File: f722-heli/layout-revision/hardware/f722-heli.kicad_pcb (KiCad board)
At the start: 6 copper layers, 41.7 x 25.4 mm, 156 parts, among them J1 USB4145-03-0170-C, J10 PORT B / JST GH, J11 PORT C / JST GH, J12 DSM / JST ZH, J2 S1 / GND-VX-S, J3 S2 / GND-VX-S, J4 S3 / GND-VX-S, J5 TAIL / GND-VX-S, J6 ESC / GND-VX-S, J7 RPM / GND-VX-S, J8 SBUS / GND-VX-S, J9 PORT A / JST GH, Q1 BSS138LT1G, Q2 BSS138LT1G, SW1 BOOT / KMT031NGJLHS, U1 STM32F722RET6, U10 TPS2553DRVR / USB input limit, U11 TPS2553DRVR / DSM output limit, U12 USBLC6-4SC6 / header clamp, U13 USBLC6-4SC6 / header clamp, U14 TPD4E05U06DQAR / UART ESD, U15 TPD4E05U06DQAR / UART ESD, U16 PESD15VS2UT,215 / 15V ESD, U2 ICM-42688-P, U3 W25N01GVZEIG / 128MiB, U4 DPS368XTSA1 / 0x76, U5 TPS259472ARPWR, U6 TPS63070RNMR / nominal 5.088V, U7 TPS2117DRLR / ABC priority mux, U8 TPS2121RUXR / BEC-priority co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, U9 TPS62162DSGR / 3.3V 1A, Y1 8MHz / CL10pF / TAXM8M4RDBCCT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

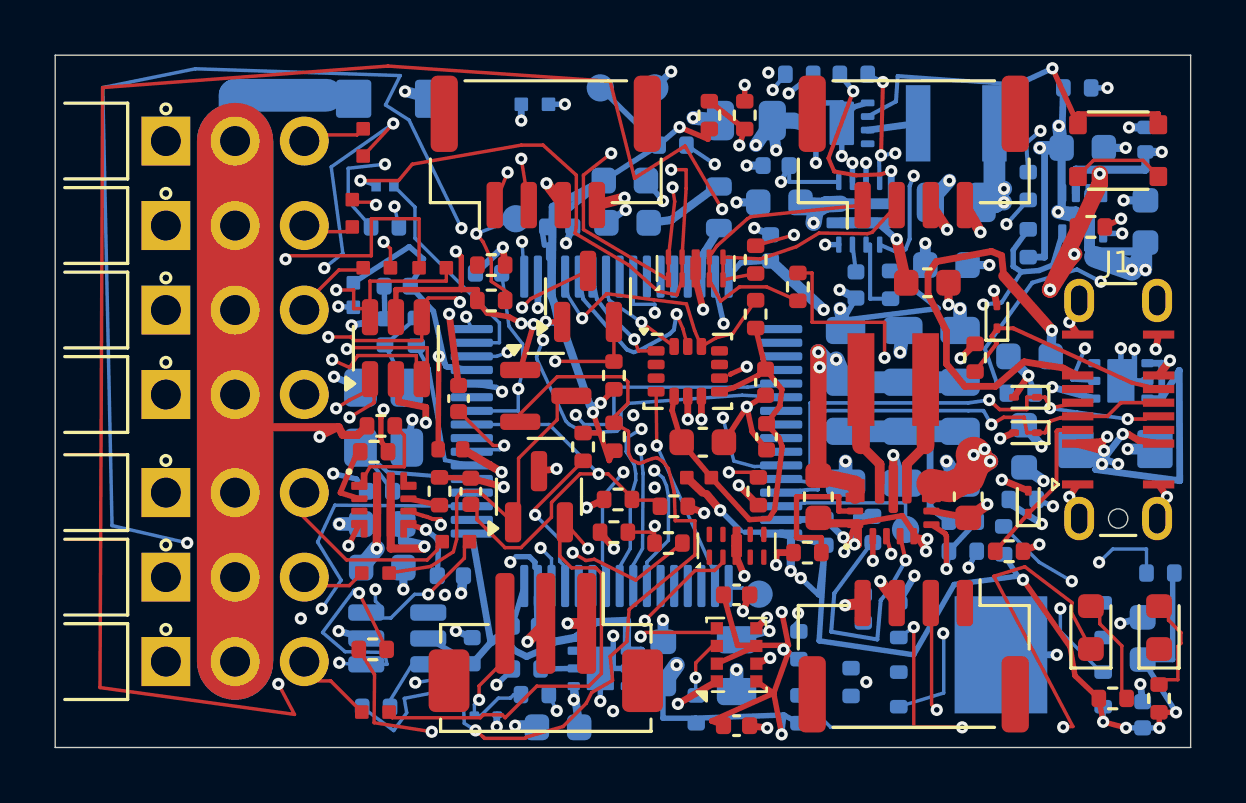
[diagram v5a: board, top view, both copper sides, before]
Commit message: WIP: checkpoint F722 at 11 unfinished connections
Native geometry/parity/ERC clean. Current numerical power/VCAP and complete electrical qualification pending. Not for manufacture or flight.
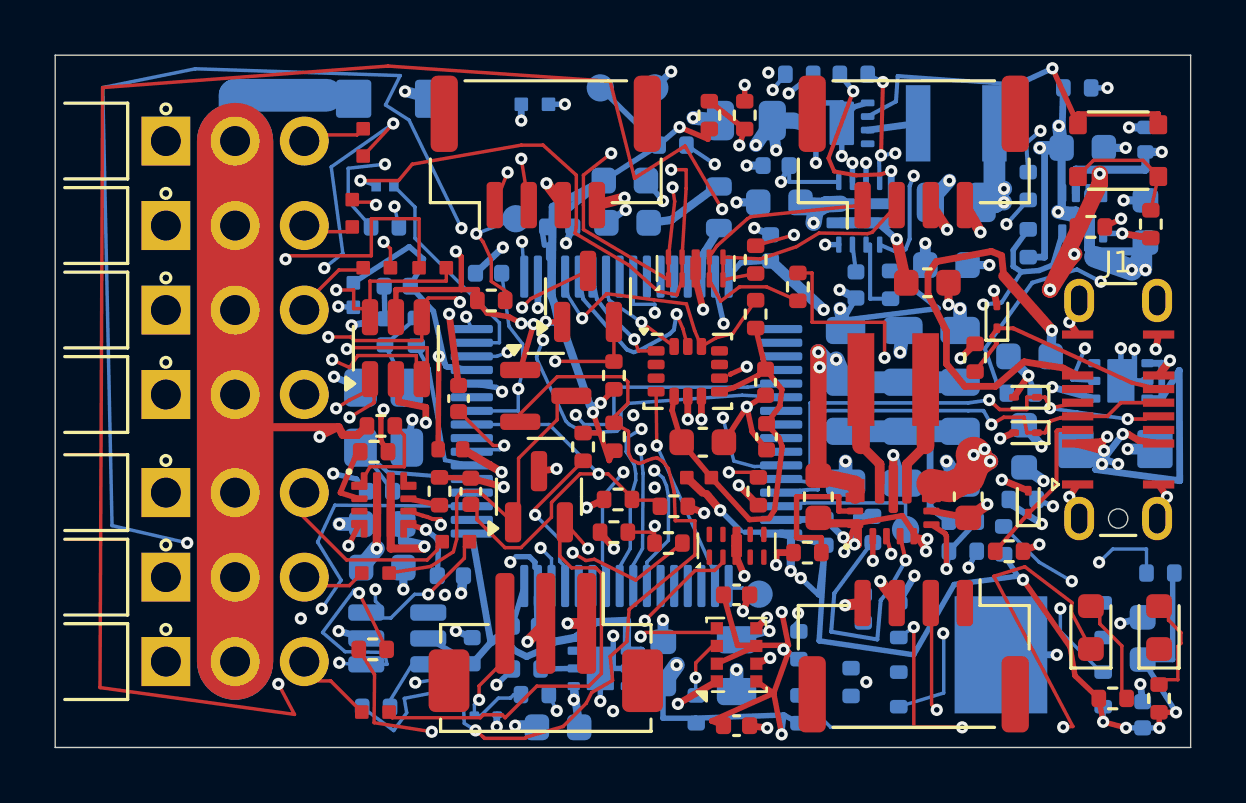
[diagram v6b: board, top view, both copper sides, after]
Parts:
- moved R2 24.2 mm to (40.2, 6.20), turned to -90 degrees
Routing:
- net BOOT0: track 2.89 -> 4.16 mm
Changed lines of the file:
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@@
 	(footprint "F722_Heli:R_0402_1005Metric"
 		(layer "F.Cu")
-		(at 16 7.7)
+		(at 40.2 6.2 -90)
 		(descr "Resistor SMD 0402 (1005 Metric), square (rectangular) end terminal, IPC-7351 nominal, (Body size source: IPC-SM-782 page 72, https://www.pcb-3d.com/wordpress/wp-content/uploads/ipc-sm-782a_amendment_1_and_2.pdf), generated with kicad-footprint-generator")
 		(tags "resistor")
 		(property "Reference" "R2"
-			(at 0 -1.17 180)
+			(at 0 -1.17 90)
 			(layer "F.SilkS")
 			(hide yes)
@@
 		)
 		(property "Value" "2.2k / 1%"
-			(at 0 1.17 180)
+			(at 0 1.17 90)
 			(layer "F.Fab")
 			(hide yes)
@@
 		)
 		(property "Datasheet" ""
-			(at 0 0 180)
+			(at 0 0 90)
 			(layer "F.Fab")
 			(hide yes)
@@
 		)
 		(property "Description" ""
-			(at 0 0 180)
+			(at 0 0 90)
 			(layer "F.Fab")
 			(hide yes)
@@
 		)
 		(property "MPN" "0402WGF2201TCE"
-			(at 0 0 0)
+			(at 0 0 270)
 			(layer "F.Fab")
 			(hide yes)
@@
 		)
 		(property "Manufacturer" "UNI-ROYAL (Uniroyal Elec)"
-			(at 0 0 0)
+			(at 0 0 270)
 			(layer "F.Fab")
 			(hide yes)
@@
 		)
 		(property "LCSC" "C25879"
-			(at 0 0 0)
+			(at 0 0 270)
 			(layer "F.Fab")
 			(hide yes)
@@
 		)
 		(property "Supplier" "https://jlcpcb.com/partdetail/26622-0402WGF2201TCE/C25879"
-			(at 0 0 0)
+			(at 0 0 270)
 			(layer "F.Fab")
 			(hide yes)
@@
 		(duplicate_pad_numbers_are_jumpers no)
 		(fp_line
-			(start -0.153641 -0.38)
-			(end 0.153641 -0.38)
+			(start -0.153641 0.38)
+			(end 0.153641 0.38)
 			(stroke
 				(width 0.12)
@@
 		)
 		(fp_line
-			(start -0.153641 0.38)
-			(end 0.153641 0.38)
+			(start -0.153641 -0.38)
+			(end 0.153641 -0.38)
 			(stroke
 				(width 0.12)
@@
 		)
 		(fp_line
-			(start -0.93 -0.47)
-			(end 0.93 -0.47)
+			(start -0.93 0.47)
+			(end -0.93 -0.47)
 			(stroke
 				(width 0.05)
@@
 		)
 		(fp_line
-			(start -0.93 0.47)
-			(end -0.93 -0.47)
+			(start 0.93 0.47)
+			(end -0.93 0.47)
 			(stroke
 				(width 0.05)
@@
 		)
 		(fp_line
-			(start 0.93 -0.47)
-			(end 0.93 0.47)
+			(start -0.93 -0.47)
+			(end 0.93 -0.47)
 			(stroke
 				(width 0.05)
@@
 		)
 		(fp_line
-			(start 0.93 0.47)
-			(end -0.93 0.47)
+			(start 0.93 -0.47)
+			(end 0.93 0.47)
 			(stroke
 				(width 0.05)
@@
 		)
 		(fp_line
-			(start -0.525 -0.27)
-			(end 0.525 -0.27)
+			(start -0.525 0.27)
+			(end -0.525 -0.27)
 			(stroke
 				(width 0.1)
@@
 		)
 		(fp_line
-			(start -0.525 0.27)
-			(end -0.525 -0.27)
+			(start 0.525 0.27)
+			(end -0.525 0.27)
 			(stroke
 				(width 0.1)
@@
 		)
 		(fp_line
-			(start 0.525 -0.27)
-			(end 0.525 0.27)
+			(start -0.525 -0.27)
+			(end 0.525 -0.27)
 			(stroke
 				(width 0.1)
@@
 		)
 		(fp_line
-			(start 0.525 0.27)
-			(end -0.525 0.27)
+			(start 0.525 -0.27)
+			(end 0.525 0.27)
 			(stroke
 				(width 0.1)
@@
 		)
 		(fp_text user "${REFERENCE}"
-			(at 0 0 180)
+			(at 0 0 90)
 			(layer "F.Fab")
 			(effects
@@
 		)
 		(pad "1" smd roundrect
-			(at -0.51 0)
+			(at -0.51 0 270)
 			(size 0.54 0.64)
 			(layers "F.Cu" "F.Mask" "F.Paste")
@@
 		)
 		(pad "2" smd roundrect
-			(at 0.51 0)
+			(at 0.51 0 270)
 			(size 0.54 0.64)
 			(layers "F.Cu" "F.Mask" "F.Paste")
@@
 	)
 	(segment
-		(start 16.51 7.7)
-		(end 16.4252 7.0556)
-		(width 0.25)
-		(layer "F.Cu")
-		(net "GND")
-	)
-	(segment
 		(start 24.275 22.975)
 		(end 22.8461 23.8)
@@
 	)
 	(segment
+		(start 40.2 6.71)
+		(end 39.15 6.54)
+		(width 0.25)
+		(layer "F.Cu")
+		(net "GND")
+	)
+	(segment
 		(start 25.725 21.025)
 		(end 26.1139 20.6361)
@@
 		(width 0.127)
 		(layer "F.Cu")
+		(net "BOOT0")
+	)
+	(segment
+		(start 40.2 5.69)
+		(end 40.475 4.45)
+		(width 0.127)
+		(layer "F.Cu")
